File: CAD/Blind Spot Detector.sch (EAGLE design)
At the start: 11 parts

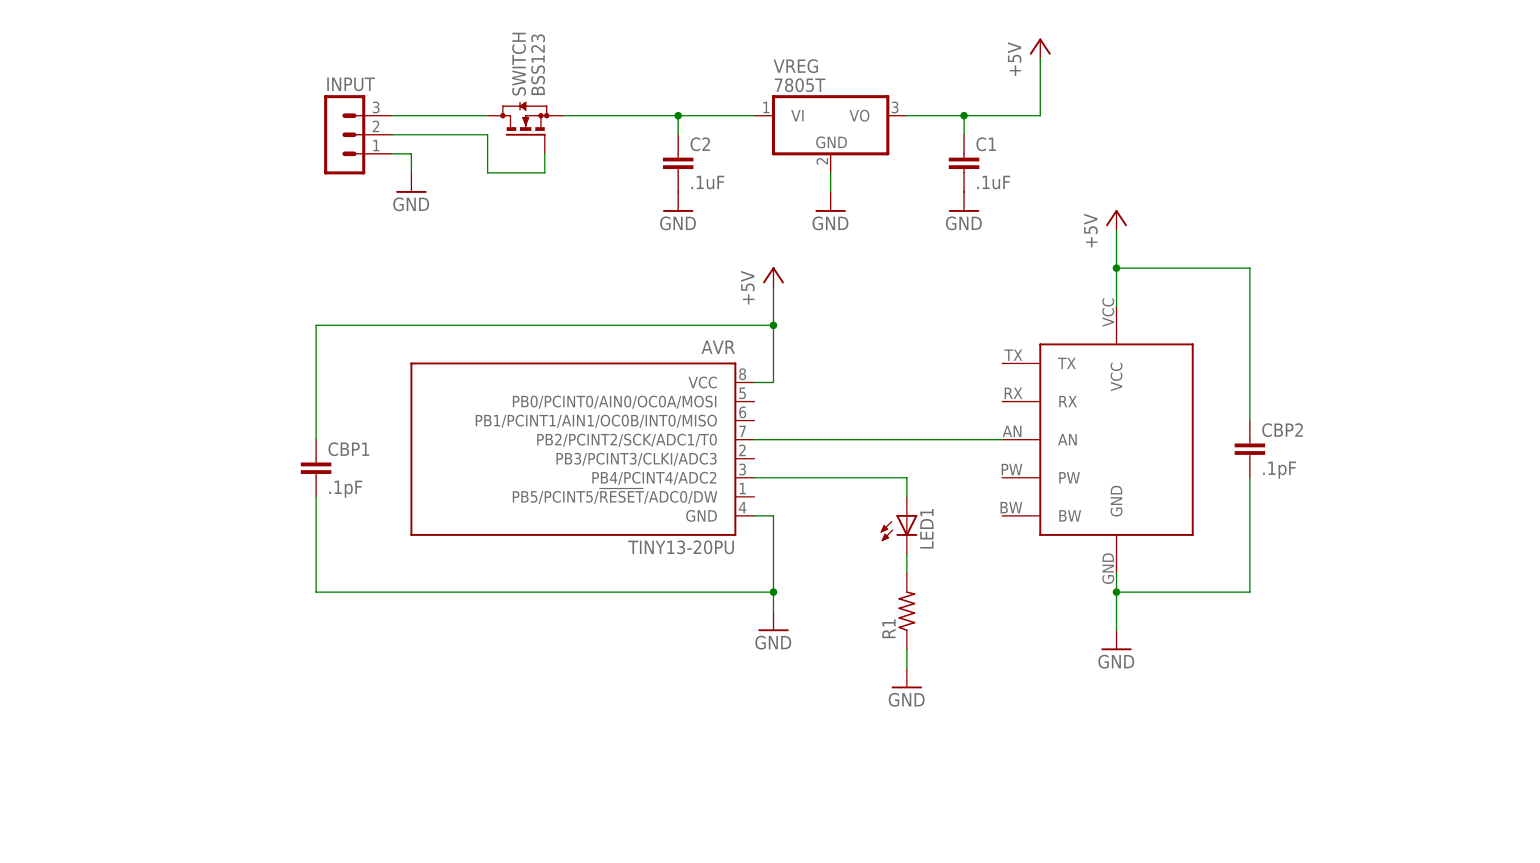
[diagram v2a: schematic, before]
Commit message: Updated connections
Changed sensor connections to pin headers to main board
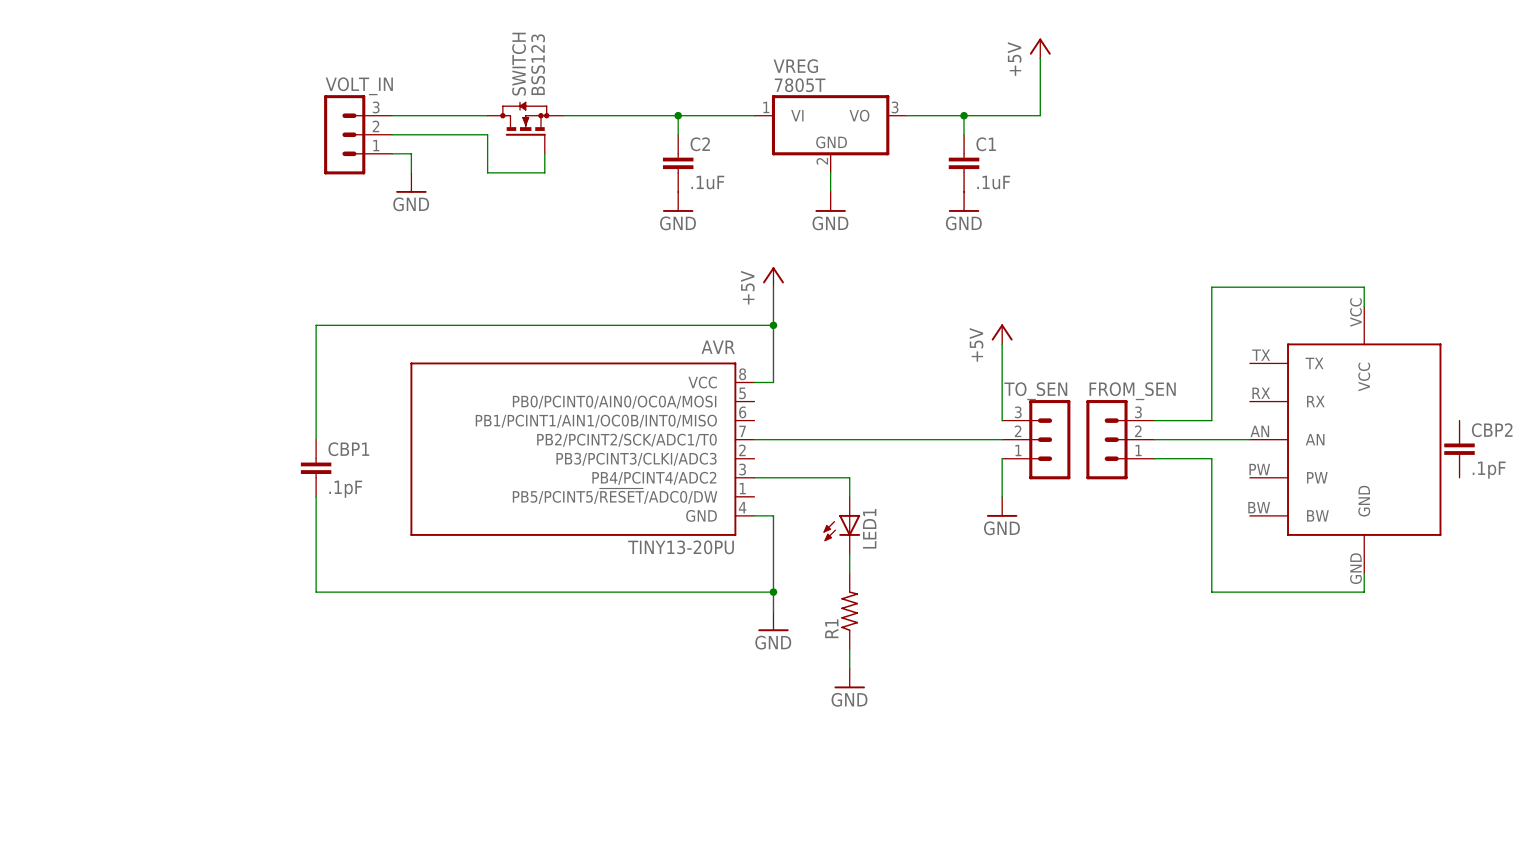
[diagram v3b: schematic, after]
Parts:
- added FROM_SEN, TO_SEN: (no value), con-lstb:MA03-1
- renumbered INPUT to VOLT_IN
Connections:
- new net N$5: FROM_SEN.1, ULTRA_SEN.GND
- new net N$6: FROM_SEN.3, ULTRA_SEN.VCC
- new net N$8: AVR.PB2/PCINT2/SCK/ADC1/T0, TO_SEN.2
- net +5V: now also TO_SEN.3; no longer CBP2.1, ULTRA_SEN.VCC
- net GND: now also TO_SEN.1; no longer CBP2.2, ULTRA_SEN.GND
- net N$2: now also FROM_SEN.2; no longer AVR.PB2/PCINT2/SCK/ADC1/T0
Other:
- moved on the sheet: CBP2, LED1, R1
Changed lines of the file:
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@@
 <part name="ULTRA_SEN" library="Ultrasonic_sensor" deviceset="ULTRASONIC_SENSOR" device=""/>
 <part name="AVR" library="atmel" deviceset="TINY13" device="PU" technology="-20"/>
-<part name="P+1" library="supply1" deviceset="+5V" device=""/>
 <part name="P+2" library="supply1" deviceset="+5V" device=""/>
 <part name="GND1" library="supply1" deviceset="GND" device=""/>
-<part name="GND2" library="supply1" deviceset="GND" device=""/>
 <part name="CBP1" library="rcl" deviceset="C-EU" device="C0805" value=".1pF"/>
 <part name="CBP2" library="rcl" deviceset="C-EU" device="C0805" value=".1pF"/>
@@
 <part name="SWITCH" library="transistor-small-signal" deviceset="BSS123" device=""/>
 <part name="LED1" library="led" deviceset="LED" device="5MM"/>
-<part name="INPUT" library="con-lstb" deviceset="MA03-1" device=""/>
+<part name="VOLT_IN" library="con-lstb" deviceset="MA03-1" device=""/>
 <part name="GND7" library="supply1" deviceset="GND" device=""/>
+<part name="FROM_SEN" library="con-lstb" deviceset="MA03-1" device=""/>
+<part name="TO_SEN" library="con-lstb" deviceset="MA03-1" device=""/>
+<part name="GND2" library="supply1" deviceset="GND" device=""/>
+<part name="P+1" library="supply1" deviceset="+5V" device=""/>
 </parts>
 <sheets>
@@
 </plain>
 <instances>
-<instance part="ULTRA_SEN" gate="G$1" x="119.38" y="43.18"/>
+<instance part="ULTRA_SEN" gate="G$1" x="152.4" y="43.18"/>
 <instance part="AVR" gate="G$1" x="53.34" y="43.18" rot="MR0"/>
-<instance part="P+1" gate="1" x="121.92" y="78.74"/>
 <instance part="P+2" gate="1" x="76.2" y="71.12"/>
 <instance part="GND1" gate="1" x="76.2" y="22.86"/>
-<instance part="GND2" gate="1" x="121.92" y="20.32"/>
 <instance part="CBP1" gate="G$1" x="15.24" y="45.72"/>
-<instance part="CBP2" gate="G$1" x="139.7" y="48.26"/>
+<instance part="CBP2" gate="G$1" x="167.64" y="48.26"/>
 <instance part="C1" gate="G$1" x="101.6" y="86.36"/>
 <instance part="C2" gate="G$1" x="63.5" y="86.36"/>
@@
 <instance part="GND5" gate="1" x="83.82" y="78.74"/>
 <instance part="P+3" gate="1" x="111.76" y="101.6"/>
-<instance part="R1" gate="G$1" x="93.98" y="25.4" rot="R90"/>
+<instance part="R1" gate="G$1" x="86.36" y="25.4" rot="R90"/>
 <instance part="VREG" gate="A1" x="83.82" y="91.44"/>
-<instance part="GND6" gate="1" x="93.98" y="15.24"/>
+<instance part="GND6" gate="1" x="86.36" y="15.24"/>
 <instance part="SWITCH" gate="G$1" x="43.18" y="91.44" rot="R90"/>
-<instance part="LED1" gate="G$1" x="93.98" y="38.1"/>
-<instance part="INPUT" gate="G$1" x="17.78" y="88.9"/>
+<instance part="LED1" gate="G$1" x="86.36" y="38.1"/>
+<instance part="VOLT_IN" gate="G$1" x="17.78" y="88.9"/>
 <instance part="GND7" gate="1" x="27.94" y="81.28"/>
+<instance part="FROM_SEN" gate="G$1" x="119.38" y="48.26"/>
+<instance part="TO_SEN" gate="G$1" x="114.3" y="48.26" rot="MR0"/>
+<instance part="GND2" gate="1" x="106.68" y="38.1"/>
+<instance part="P+1" gate="1" x="106.68" y="63.5"/>
 </instances>
 <busses>
@@
 <nets>
 <net name="+5V" class="0">
-<segment>
-<pinref part="ULTRA_SEN" gate="G$1" pin="VCC"/>
-<wire x1="121.92" y1="66.04" x2="121.92" y2="71.12" width="0.1524" layer="91"/>
-<pinref part="P+1" gate="1" pin="+5V"/>
-<pinref part="CBP2" gate="G$1" pin="1"/>
-<wire x1="121.92" y1="71.12" x2="121.92" y2="76.2" width="0.1524" layer="91"/>
-<wire x1="121.92" y1="71.12" x2="139.7" y2="71.12" width="0.1524" layer="91"/>
-<wire x1="139.7" y1="71.12" x2="139.7" y2="50.8" width="0.1524" layer="91"/>
-<junction x="121.92" y="71.12"/>
-</segment>
 <segment>
 <pinref part="AVR" gate="G$1" pin="VCC"/>
@@
 <pinref part="VREG" gate="A1" pin="VO"/>
 </segment>
+<segment>
+<pinref part="TO_SEN" gate="G$1" pin="3"/>
+<wire x1="106.68" y1="50.8" x2="106.68" y2="60.96" width="0.1524" layer="91"/>
+<pinref part="P+1" gate="1" pin="+5V"/>
+</segment>
 </net>
 <net name="GND" class="0">
-<segment>
-<pinref part="GND2" gate="1" pin="GND"/>
-<pinref part="ULTRA_SEN" gate="G$1" pin="GND"/>
-<wire x1="121.92" y1="30.48" x2="121.92" y2="27.94" width="0.1524" layer="91"/>
-<pinref part="CBP2" gate="G$1" pin="2"/>
-<wire x1="121.92" y1="27.94" x2="121.92" y2="22.86" width="0.1524" layer="91"/>
-<wire x1="139.7" y1="43.18" x2="139.7" y2="27.94" width="0.1524" layer="91"/>
-<wire x1="139.7" y1="27.94" x2="121.92" y2="27.94" width="0.1524" layer="91"/>
-<junction x="121.92" y="27.94"/>
-</segment>
 <segment>
 <pinref part="AVR" gate="G$1" pin="GND"/>
@@
 <pinref part="R1" gate="G$1" pin="1"/>
 <pinref part="GND6" gate="1" pin="GND"/>
-<wire x1="93.98" y1="20.32" x2="93.98" y2="17.78" width="0.1524" layer="91"/>
-</segment>
-<segment>
-<pinref part="INPUT" gate="G$1" pin="1"/>
+<wire x1="86.36" y1="20.32" x2="86.36" y2="17.78" width="0.1524" layer="91"/>
+</segment>
+<segment>
+<pinref part="VOLT_IN" gate="G$1" pin="1"/>
 <wire x1="25.4" y1="86.36" x2="27.94" y2="86.36" width="0.1524" layer="91"/>
 <wire x1="27.94" y1="86.36" x2="27.94" y2="83.82" width="0.1524" layer="91"/>
 <pinref part="GND7" gate="1" pin="GND"/>
+</segment>
+<segment>
+<pinref part="TO_SEN" gate="G$1" pin="1"/>
+<wire x1="106.68" y1="45.72" x2="106.68" y2="40.64" width="0.1524" layer="91"/>
+<pinref part="GND2" gate="1" pin="GND"/>
 </segment>
 </net>
@@
 </segment>
 </net>
-<net name="N$2" class="0">
-<segment>
-<pinref part="ULTRA_SEN" gate="G$1" pin="AN"/>
-<pinref part="AVR" gate="G$1" pin="PB2/PCINT2/SCK/ADC1/T0"/>
-<wire x1="106.68" y1="48.26" x2="73.66" y2="48.26" width="0.1524" layer="91"/>
-</segment>
-</net>
 <net name="N$4" class="0">
 <segment>
 <pinref part="AVR" gate="G$1" pin="PB4/PCINT4/ADC2"/>
-<wire x1="93.98" y1="43.18" x2="73.66" y2="43.18" width="0.1524" layer="91"/>
-<wire x1="93.98" y1="40.64" x2="93.98" y2="43.18" width="0.1524" layer="91"/>
+<wire x1="86.36" y1="43.18" x2="73.66" y2="43.18" width="0.1524" layer="91"/>
+<wire x1="86.36" y1="40.64" x2="86.36" y2="43.18" width="0.1524" layer="91"/>
 <pinref part="LED1" gate="G$1" pin="A"/>
 </segment>
@@
 <wire x1="38.1" y1="88.9" x2="38.1" y2="83.82" width="0.1524" layer="91"/>
 <wire x1="38.1" y1="83.82" x2="45.72" y2="83.82" width="0.1524" layer="91"/>
-<pinref part="INPUT" gate="G$1" pin="2"/>
+<pinref part="VOLT_IN" gate="G$1" pin="2"/>
 <wire x1="25.4" y1="88.9" x2="38.1" y2="88.9" width="0.1524" layer="91"/>
 </segment>
@@
 <segment>
 <pinref part="R1" gate="G$1" pin="2"/>
-<wire x1="93.98" y1="33.02" x2="93.98" y2="30.48" width="0.1524" layer="91"/>
+<wire x1="86.36" y1="33.02" x2="86.36" y2="30.48" width="0.1524" layer="91"/>
 <pinref part="LED1" gate="G$1" pin="C"/>
 </segment>
@@
 <net name="BATTERY" class="0">
 <segment>
-<pinref part="INPUT" gate="G$1" pin="3"/>
+<pinref part="VOLT_IN" gate="G$1" pin="3"/>
 <pinref part="SWITCH" gate="G$1" pin="D"/>
 <wire x1="25.4" y1="91.44" x2="38.1" y2="91.44" width="0.1524" layer="91"/>
 </segment>
 </net>
+<net name="N$2" class="0">
+<segment>
+<pinref part="ULTRA_SEN" gate="G$1" pin="AN"/>
+<pinref part="FROM_SEN" gate="G$1" pin="2"/>
+<wire x1="139.7" y1="48.26" x2="127" y2="48.26" width="0.1524" layer="91"/>
+</segment>
+</net>
+<net name="N$6" class="0">
+<segment>
+<pinref part="FROM_SEN" gate="G$1" pin="3"/>
+<wire x1="127" y1="50.8" x2="134.62" y2="50.8" width="0.1524" layer="91"/>
+<wire x1="134.62" y1="68.58" x2="134.62" y2="50.8" width="0.1524" layer="91"/>
+<pinref part="ULTRA_SEN" gate="G$1" pin="VCC"/>
+<wire x1="154.94" y1="66.04" x2="154.94" y2="68.58" width="0.1524" layer="91"/>
+<wire x1="154.94" y1="68.58" x2="134.62" y2="68.58" width="0.1524" layer="91"/>
+</segment>
+</net>
+<net name="N$5" class="0">
+<segment>
+<pinref part="ULTRA_SEN" gate="G$1" pin="GND"/>
+<wire x1="154.94" y1="30.48" x2="154.94" y2="27.94" width="0.1524" layer="91"/>
+<wire x1="154.94" y1="27.94" x2="134.62" y2="27.94" width="0.1524" layer="91"/>
+<pinref part="FROM_SEN" gate="G$1" pin="1"/>
+<wire x1="134.62" y1="45.72" x2="127" y2="45.72" width="0.1524" layer="91"/>
+<wire x1="134.62" y1="27.94" x2="134.62" y2="45.72" width="0.1524" layer="91"/>
+</segment>
+</net>
+<net name="N$8" class="0">
+<segment>
+<pinref part="TO_SEN" gate="G$1" pin="2"/>
+<pinref part="AVR" gate="G$1" pin="PB2/PCINT2/SCK/ADC1/T0"/>
+<wire x1="106.68" y1="48.26" x2="73.66" y2="48.26" width="0.1524" layer="91"/>
+</segment>
+</net>

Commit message: Removed sensor
Removed sensor from schematic since it is a board of its own and will
not be on the PCB.  Also added a frame.
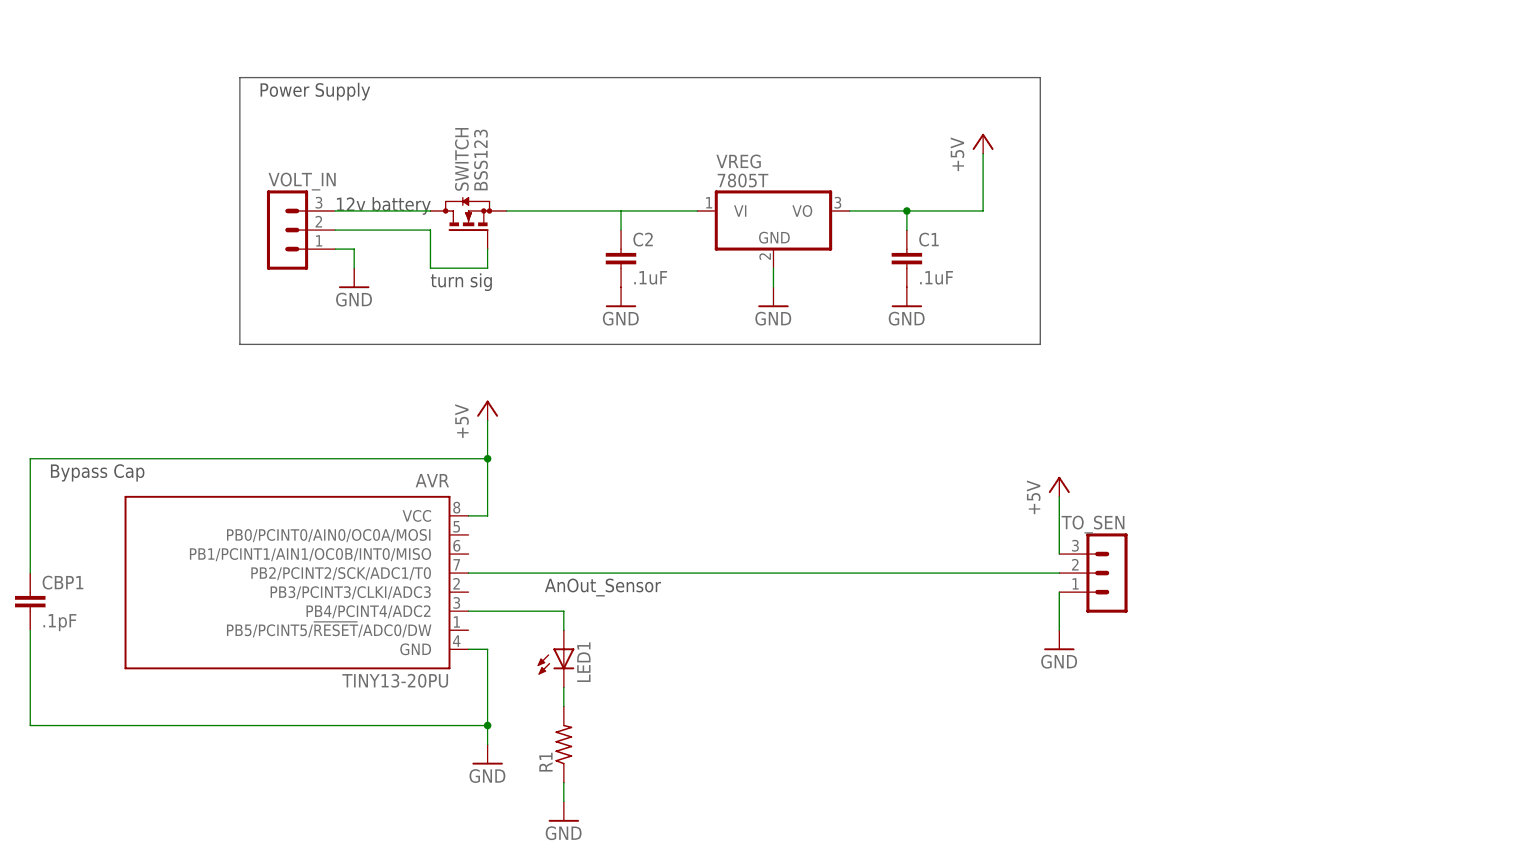
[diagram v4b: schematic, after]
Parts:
- removed CBP2: .1pF, rcl:C-EUC0805
- removed FROM_SEN: (no value), con-lstb:MA03-1
- removed ULTRA_SEN: ULTRASONIC_SENSOR, Ultrasonic_sensor:ULTRASONIC_SENSOR
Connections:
- removed net N$5: FROM_SEN.1, ULTRA_SEN.GND
- removed net N$6: FROM_SEN.3, ULTRA_SEN.VCC
- net N$1: no longer C2.1
- net N$2: now also C2.1; no longer FROM_SEN.2, ULTRA_SEN.AN
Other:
- note added: "12v battery"
- note added: "AnOut_Sensor"
- note added: "Bypass Cap"
- note added: "Power Supply"
- note added: "turn sig"
- moved on the sheet: AVR, C1, C2, CBP1, LED1, R1, SWITCH, TO_SEN, VOLT_IN, VREG
